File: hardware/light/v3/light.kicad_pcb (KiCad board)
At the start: 2 copper layers, 30 x 30 mm, 18 parts, among them J1 PH2-16-UA, J2 Conn_01x09, J3 Conn_01x09, J4 B3B-XH-A, Q1 DMG2301L, Q2 MMBT3904, U1 LP2985-50DBVR, U2 SN74LVC1G17DBVR

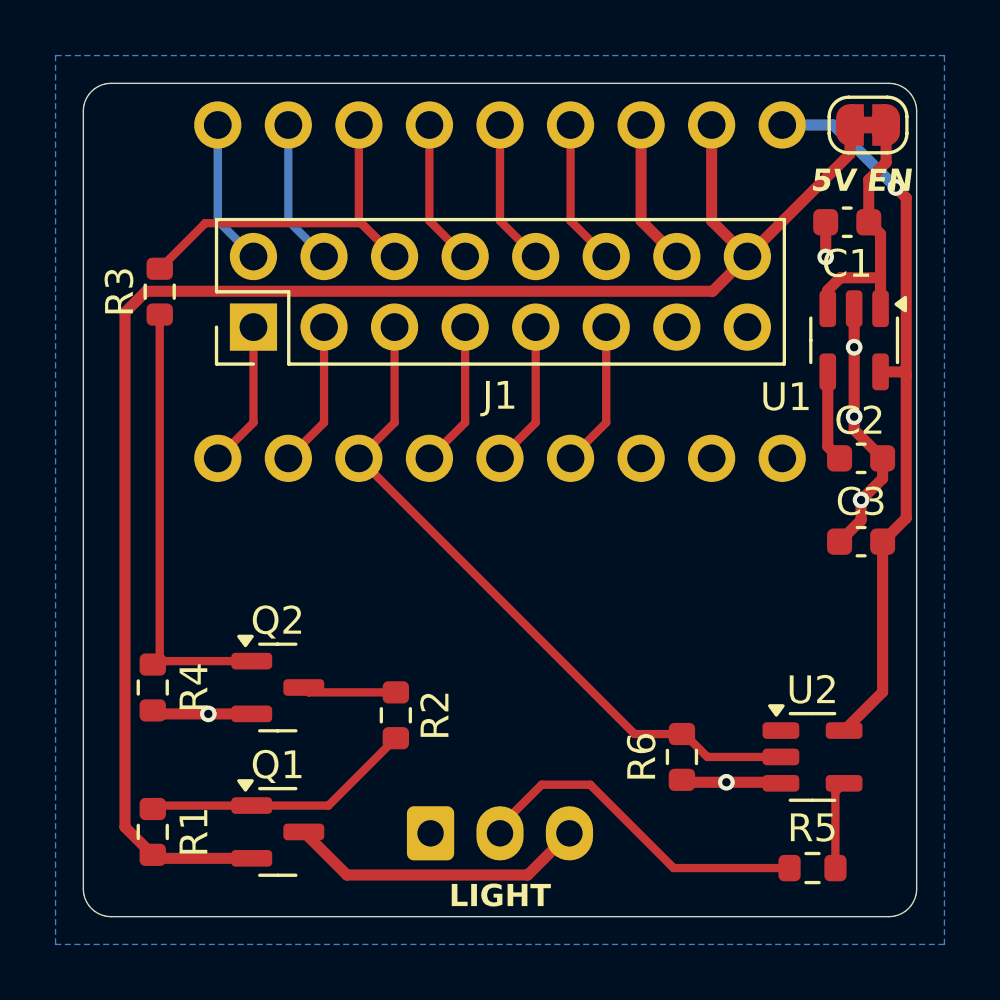
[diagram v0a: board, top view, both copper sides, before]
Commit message: Add a connector for input controls.
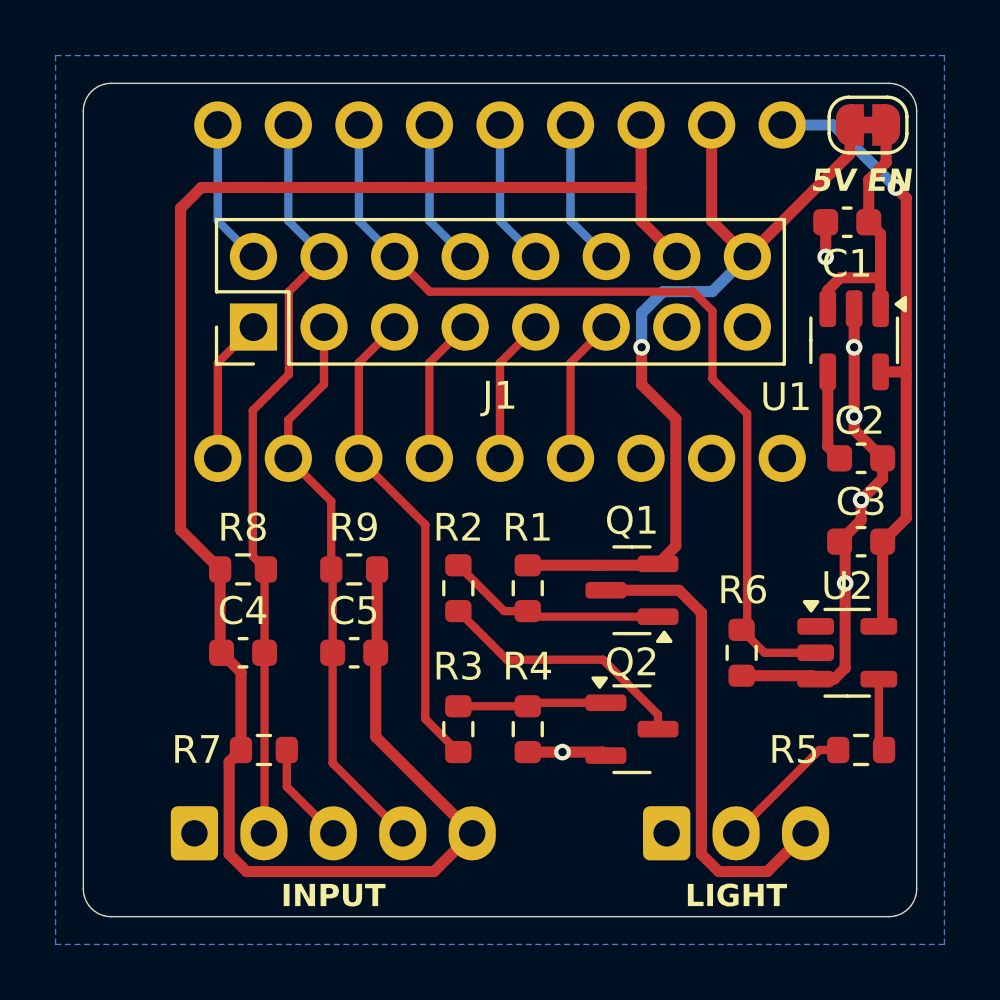
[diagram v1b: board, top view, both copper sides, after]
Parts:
- added C4: 10n, Capacitor_SMD:C_0603_1608Metric, F.Cu at (105.8, 120.5)
- added C5: 10n, Capacitor_SMD:C_0603_1608Metric, F.Cu at (109.8, 120.5)
- added J5: B5B-XH-A, Connector_JST:JST_XH_B5B-XH-A_1x05_P2.50mm_Vertical, B.Cu at (104.0, 127.0)
- added R7: 10K, Resistor_SMD:R_0603_1608Metric, F.Cu at (106.5, 124.0)
- added R8: 100K, Resistor_SMD:R_0603_1608Metric, F.Cu at (105.8, 117.5)
- added R9: 100K, Resistor_SMD:R_0603_1608Metric, F.Cu at (109.8, 117.5)
- R2: value 1K -> 10K
- moved R3 19.1 mm to (113.5, 123.2), turned to -90 degrees
- moved R1 16.1 mm to (116.0, 118.2), turned to -90 degrees
- moved Q1 15.4 mm to (119.8, 118.2), turned to 180 degrees
- moved R4 13.6 mm to (116.0, 123.2)
- moved Q2 12.8 mm to (119.8, 123.2)
- moved J4 8.50 mm to (121.0, 127.0)
- moved R2 5.10 mm to (113.5, 118.2), turned to 90 degrees
- moved R5 4.60 mm to (128.0, 124.0)
- moved R6 4.32 mm to (123.7, 120.5)
- moved U2 3.95 mm to (127.5, 120.5)
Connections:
- R3 pad 2: GPIO5 -> GPIO6
- R6 pad 2: GPIO6 -> GPIO5
- U2 pad 2: GPIO6 -> GPIO5
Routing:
- net +3.3V: track 5.27 -> 67.0 mm
- net +12V: track 58.2 -> 30.7 mm, vias 0 -> 1
- net GPIO0: track 5.27 -> 27.3 mm
- net GPIO5: track 14.9 -> 32.6 mm
- net GPIO1: track 5.26 -> 20.5 mm
- net Net-(Q2-B): track 15.8 -> 5.36 mm
- net GPIO6: track 24.7 -> 17.3 mm
- net /DATA: track 12.3 -> 4.92 mm
- net /LOAD: track 10.8 -> 17.0 mm
- net Net-(Q2-C): track 3.38 -> 9.25 mm
- net GND: track 17.5 -> 22.2 mm
- net +5V: track 26.6 -> 22.4 mm
- net /PH: track 0.00 -> 3.69 mm
- net Net-(Q1-G): track 9.63 -> 7.95 mm
- net Net-(R5-Pad2): track 3.18 -> 2.63 mm
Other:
- board text added: "${COMPANY} ${TITLE} ${ISSUE_DATE}, ${REVISION} ${COMMENT1}"
- board text added: "INPUT"
- board text added: "INPUT 3V3 IO1 PH IO0 GND"
- board text removed: "github.com/j9brown/minuet Brown Studios Minuet Light Accessory 2025/5, v3.0"

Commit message: Finalize light accessory for fabrication.
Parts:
- removed C4, C5: 10n, Capacitor_SMD:C_0603_1608Metric
- removed J5: B5B-XH-A, Connector_JST:JST_XH_B5B-XH-A_1x05_P2.50mm_Vertical
- removed R7: 10K, Resistor_SMD:R_0603_1608Metric
- removed R8, R9: 100K, Resistor_SMD:R_0603_1608Metric
- added PROTO: Val**, Generic:ProtoPins, F.Cu at (101.2, 128.8)
- moved R6 4.96 mm to (126.2, 124.8), turned to -90 degrees
- moved Q1 2.75 mm to (122.5, 118.2)
- moved Q2 2.75 mm to (122.5, 123.2)
- moved R1 2.75 mm to (118.8, 118.2)
- moved R2 2.75 mm to (116.2, 118.2)
- moved R3 2.75 mm to (116.2, 123.2)
- moved R4 2.75 mm to (118.8, 123.2)
- moved J4 2.25 mm to (118.8, 127.0)
- moved R5 1.06 mm to (128.8, 124.8), turned to 90 degrees
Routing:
- net +3.3V: track 67.0 -> 5.27 mm
- net GPIO0: track 27.3 -> 5.27 mm
- net GPIO1: track 20.5 -> 5.26 mm
- net /LOAD: track 17.0 -> 11.9 mm
- net GPIO5: track 32.6 -> 37.4 mm
- net /DATA: track 4.92 -> 9.33 mm
- net /PH: track 3.69 -> 0.00 mm
- net GPIO6: track 17.3 -> 19.5 mm
- net GND: track 22.2 -> 21.7 mm
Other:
- board text added: "PROTOTYPING AREA"
- board text removed: "INPUT"
- board text removed: "INPUT 3V3 IO1 PH IO0 GND"

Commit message: Add tooling holes and PCBA offsets.
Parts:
- added TH1: JLCPCB_PCBA_Tooling_Hole, Generic:JLCPCB_PCBA_Tooling_Hole, F.Cu at (101.2, 101.2)
- added TH2: JLCPCB_PCBA_Tooling_Hole, Generic:JLCPCB_PCBA_Tooling_Hole, F.Cu at (128.8, 128.8)
